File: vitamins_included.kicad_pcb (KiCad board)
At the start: 2 copper layers, 230.5 x 82 mm, 180 parts, among them J1 Speaker, J10 UTC16-G, J2 reset, J3 ISP, J4 reset, J5 Buzzer, J6 ISP, J9 UTC16-G, P3 WS2812, P4 SJ-43514-SMT, P6 WS2812, P8 SJ-43514-SMT, SW1 Socket, SW10 Socket, SW11 Socket, SW12 Socket, SW13 Socket, SW14 Socket, SW15 Socket, SW16 Socket, SW17 Socket, SW18 Socket, SW19 Socket, SW2 Socket, SW20 Socket, SW21 Socket, SW22 Socket, SW23 Socket, SW24 Socket, SW25 Socket, SW26 Socket, SW27 Socket, SW28 Socket, SW29 Socket, SW3 Socket, SW30 Socket, SW31 Socket, SW32 Socket, SW33 Socket, SW34 Socket, SW35 Socket, SW36 Socket, SW37 Socket, SW38 Socket, SW39 Socket, SW4 Socket, SW40 Socket, SW41 Socket, SW42 Socket, SW43 Socket, SW44 Socket, SW45 Socket, SW46 Socket, SW47 Socket, SW48 Socket, SW49 FSMSM, SW5 Socket, SW50 FSMSM, SW6 Socket, SW7 Socket, SW8 Socket, SW9 Socket, U1 ATMega32U4, U2 ATMega32U4, Y1 16MHz, Y2 16MHz

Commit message: Pre-cleanup
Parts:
- added J11: Conn_01x01, TestPoint:TestPoint_Pad_D1.5mm, B.Cu at (60.3, 18.9)
- added J12: Conn_01x01, TestPoint:TestPoint_Pad_D1.5mm, B.Cu at (69.9, 15.6)
- added J13: Conn_01x01, TestPoint:TestPoint_Pad_D1.5mm, B.Cu at (52.7, 6.50)
- added J14: Conn_01x01, TestPoint:TestPoint_Pad_D1.5mm, B.Cu at (61.3, 7.10)
- added J15: Conn_01x01, TestPoint:TestPoint_Pad_D1.5mm, B.Cu at (58.6, 3.30)
- added J16: Conn_01x01, TestPoint:TestPoint_Pad_D1.5mm, B.Cu at (78.0, 4.00)
- added J17: Conn_01x01, TestPoint:TestPoint_Pad_D1.5mm, B.Cu at (73.9, 8.50)
- added J18: Conn_01x01, TestPoint:TestPoint_Pad_D1.5mm, B.Cu at (175.7, 6.95)
- added J19: Conn_01x01, TestPoint:TestPoint_Pad_D1.5mm, B.Cu at (160.4, 14.8)
- added J20: Conn_01x01, TestPoint:TestPoint_Pad_D1.5mm, B.Cu at (150.1, 7.15)
- added J21: Conn_01x01, TestPoint:TestPoint_Pad_D1.5mm, B.Cu at (158.1, 7.30)
- added J22: Conn_01x01, TestPoint:TestPoint_Pad_D1.5mm, B.Cu at (156.2, 4.00)
- added J23: Conn_01x01, TestPoint:TestPoint_Pad_D1.5mm, B.Cu at (177.2, 11.4)
- added J24: Conn_01x01, TestPoint:TestPoint_Pad_D1.5mm, B.Cu at (160.7, 17.9)
- added J7: Conn_01x01, TestPoint:TestPoint_Pad_D1.5mm, B.Cu at (63.5, 17.9)
- added J8: Conn_01x01, TestPoint:TestPoint_Pad_D1.5mm, B.Cu at (167.6, 13.2)
- moved C4 1.16 mm to (55.6, 4.80), turned to 315 degrees
- moved C8 0.70 mm to (153.1, 4.30)
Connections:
- net /Right half/WD2812-in renamed /Right half/WS2812-in
- net /Right half/WD2812-out renamed /Right half/WS2812-out
- net /Right half/~RESET renamed /Right half/~Reset
- U1 pad 1: (no net) -> /Left half/PE6
- U1 pad 12: (no net) -> /Left half/PB7
- U1 pad 20: (no net) -> /Left half/PD2
- U1 pad 21: (no net) -> /Left half/PD3
- U1 pad 25: (no net) -> /Left half/PD4
- U1 pad 8: (no net) -> /Left half/PB0
- U2 pad 1: (no net) -> /Right half/PE6
- U2 pad 12: (no net) -> /Right half/PB7
- U2 pad 20: (no net) -> /Right half/PD2
- U2 pad 21: (no net) -> /Right half/PD3
- U2 pad 25: (no net) -> /Right half/PD4
- U2 pad 8: (no net) -> /Right half/PB0
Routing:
- net /Right half/SDA: track 75.6 -> 99.1 mm, vias 3 -> 4
- net /Left half/PD2: track 0.00 -> 12.0 mm, vias 0 -> 2
- net VCC: track 738.8 -> 749.7 mm
- net /Right half/PD2: track 0.00 -> 10.9 mm
- net /Right half/PD4: track 0.00 -> 7.41 mm
- net /Left half/PD3: track 0.00 -> 7.33 mm
- net /Left half/PD4: track 0.00 -> 5.10 mm
- net /Left half/PB0: track 0.00 -> 4.75 mm
- net /Right half/PB0: track 0.00 -> 4.42 mm
- net /Right half/PD3: track 0.00 -> 3.51 mm
- net VBUS: track 160.6 -> 157.5 mm
- net Net-(D35-Pad4): track 39.2 -> 36.1 mm
- net /Right half/PE6: track 0.00 -> 2.45 mm
- net /Left half/PE6: track 0.00 -> 2.42 mm
- net /Left half/MOSI: track 37.3 -> 35.3 mm
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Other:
- board text added: "-"
- board text added: "B0"
- board text added: "B7"
- board text added: "D -"
- board text added: "D2"
- board text added: "D3"
- board text added: "D4"
- board text added: "E6"
- board text removed: "+ D -"

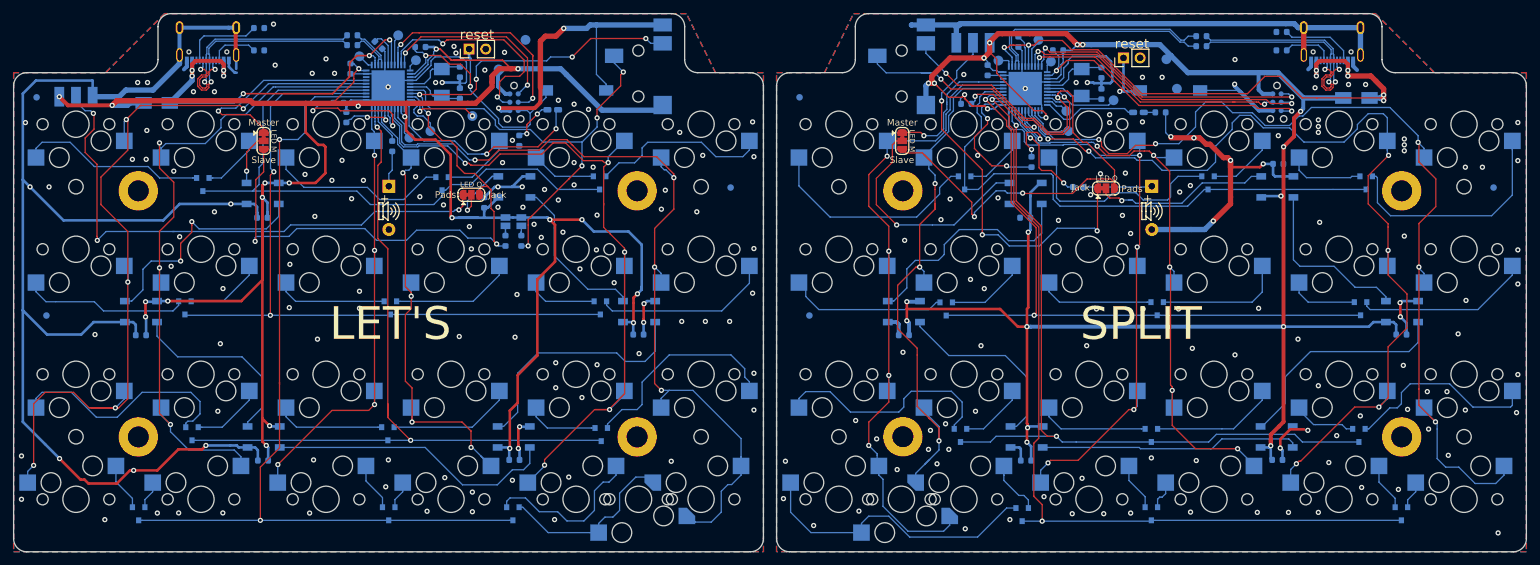
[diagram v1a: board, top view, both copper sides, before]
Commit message: Added footprint for AST1109MLTRQ buzzer
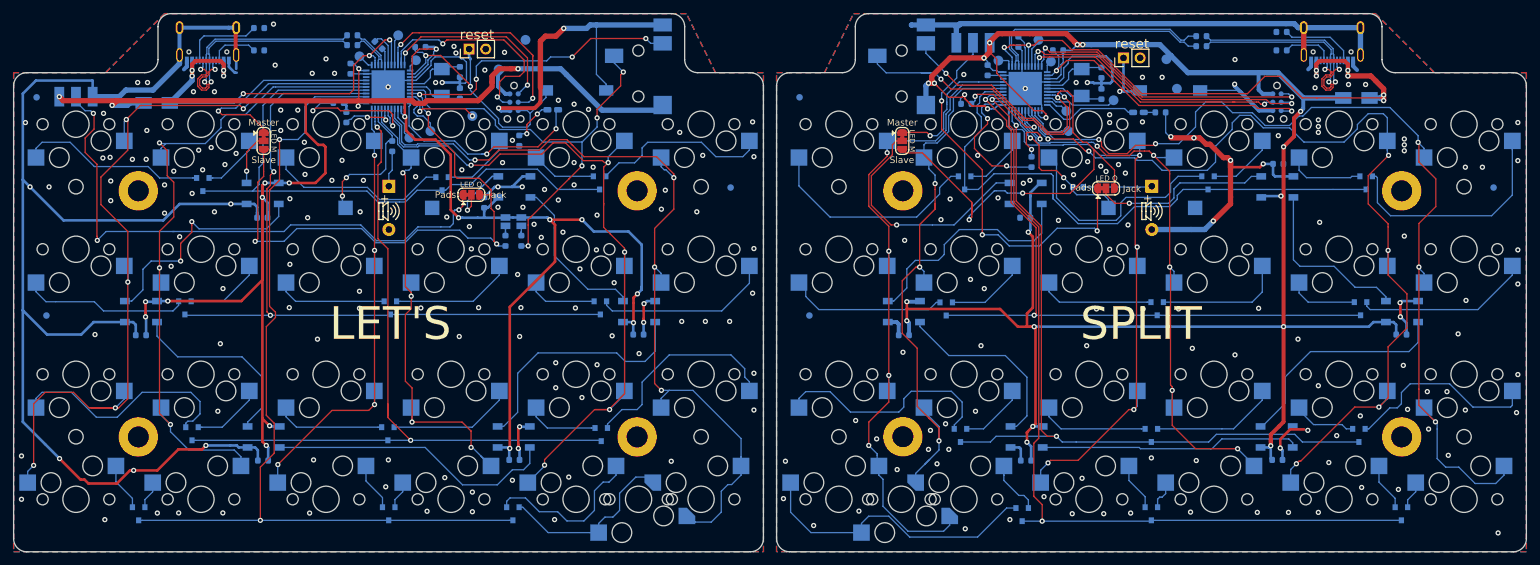
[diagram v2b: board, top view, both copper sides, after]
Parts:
- added J25: Buzzer_piezo, Buzzer_Beeper:Buzzer_Mallory_AST1109MLTRQ, B.Cu at (57.2, 29.6)
- added J26: Buzzer_piezo, Buzzer_Beeper:Buzzer_Mallory_AST1109MLTRQ, B.Cu at (173.4, 29.6)
- G*** (x2): footprint graphics:kiwi -> graphics:kiwi12.5mm
- P4, P8: footprint Connectors:SJ-4351X-SMT -> UJ31-CH-31-SMT-TR:SJ-4351X-SMT
- R1, R2, R6, R9: value 4k7 -> 4K7
- R17, R18, R19, R20: value 5k1 -> 5K1
- moved G*** 3.41 mm to (196.9, 31.7)
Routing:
- net /Left half/buzz: track 5.90 -> 23.5 mm, vias 0 -> 2
- net /Right half/buzz: track 16.7 -> 24.6 mm
- net VCC: track 749.7 -> 742.7 mm
- net /Left half/WS2812-out: track 84.7 -> 88.1 mm
- net /Right half/SDA: track 99.1 -> 102.4 mm
- net /Right half/row0: track 86.9 -> 90.2 mm
- net Net-(D14-Pad1): track 31.8 -> 34.1 mm
- net /Right half/col1: track 86.5 -> 88.2 mm
- net /Left half/row3: track 134.8 -> 136.2 mm
- net /Left half/~Reset: track 45.3 -> 43.9 mm
- net Net-(D35-Pad4): track 36.1 -> 37.2 mm
- net VBUS: track 157.5 -> 158.4 mm
- net /Left half/row0: track 95.7 -> 94.9 mm
- net GND: vias 226 -> 253
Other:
- board text added: "rev2.1"

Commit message: Modified reset switch footprint for better manufacturing, and added updated gerbers
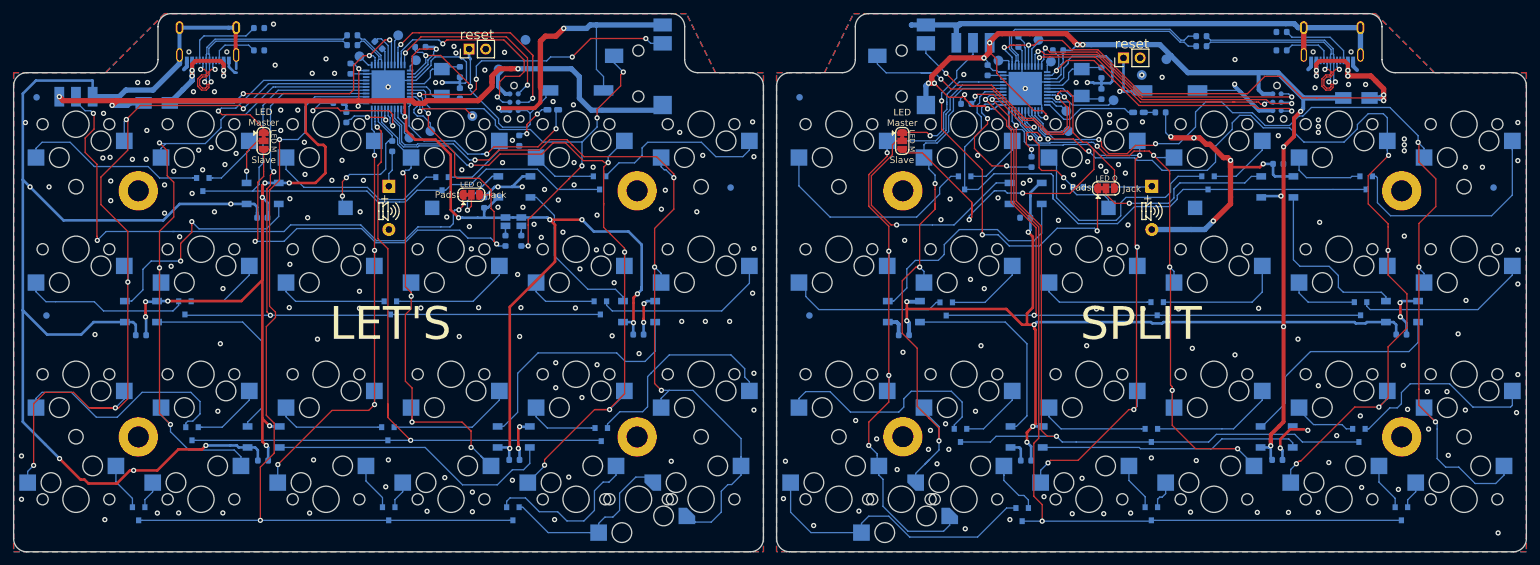
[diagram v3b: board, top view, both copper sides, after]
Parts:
- moved J23 5.75 mm to (171.9, 9.35)
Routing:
- net Net-(D36-Pad2): track 29.3 -> 31.8 mm
- net VCC: track 742.7 -> 744.6 mm
- net Net-(D30-Pad2): track 29.1 -> 31.0 mm
- net VBUS: track 158.4 -> 160.1 mm
- net Net-(D38-Pad4): track 26.6 -> 27.6 mm
- net Net-(D9-Pad2): track 32.4 -> 33.1 mm
- net GND: track 569.4 -> 569.2 mm, vias 253 -> 252
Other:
- board text added: "LED Master"
- board text removed: "Master"

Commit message: Added ESD protection to connectors
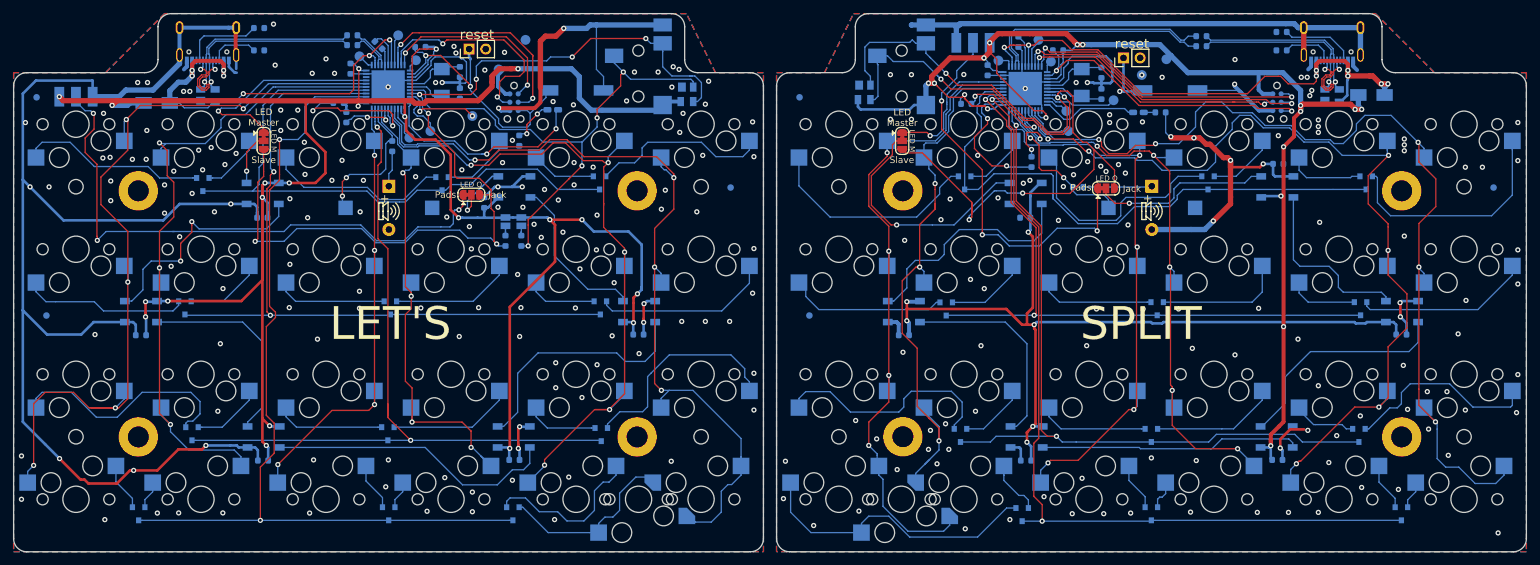
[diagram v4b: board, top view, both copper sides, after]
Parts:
- added D41: PRTR5V0U2X, Package_TO_SOT_SMD:SOT-143, B.Cu at (102.6, 12.3)
- added D42: PRTR5V0U2X, Package_TO_SOT_SMD:SOT-143, B.Cu at (29.6, 12.5)
- added D43: PRTR5V0U2X, Package_TO_SOT_SMD:SOT-143, B.Cu at (200.9, 12.5)
- added D44: PRTR5V0U2X, Package_TO_SOT_SMD:SOT-143, B.Cu at (129.6, 12.0)
- moved D26 2.34 mm to (206.9, 12.4)
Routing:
- net VCC: track 744.6 -> 767.4 mm, vias 41 -> 44
- net /Right half/SDA: track 102.4 -> 118.5 mm
- net /Left half/SDA: track 132.8 -> 147.5 mm
- net /Left half/SCL/D3: track 68.0 -> 80.1 mm
- net /Right half/SCL/D3: track 46.4 -> 52.8 mm
- net /Right half/col4: track 145.0 -> 140.1 mm
- net VBUS: track 160.1 -> 155.5 mm
- net /Right half/Dd+: track 32.6 -> 34.0 mm
- net /Right half/Dd-: track 34.1 -> 35.5 mm
- net /Left half/Dd-: track 35.5 -> 36.9 mm
- net /Left half/Dd+: track 35.0 -> 36.4 mm
- net /Right half/col5: track 146.4 -> 147.7 mm
- net GND: vias 252 -> 266

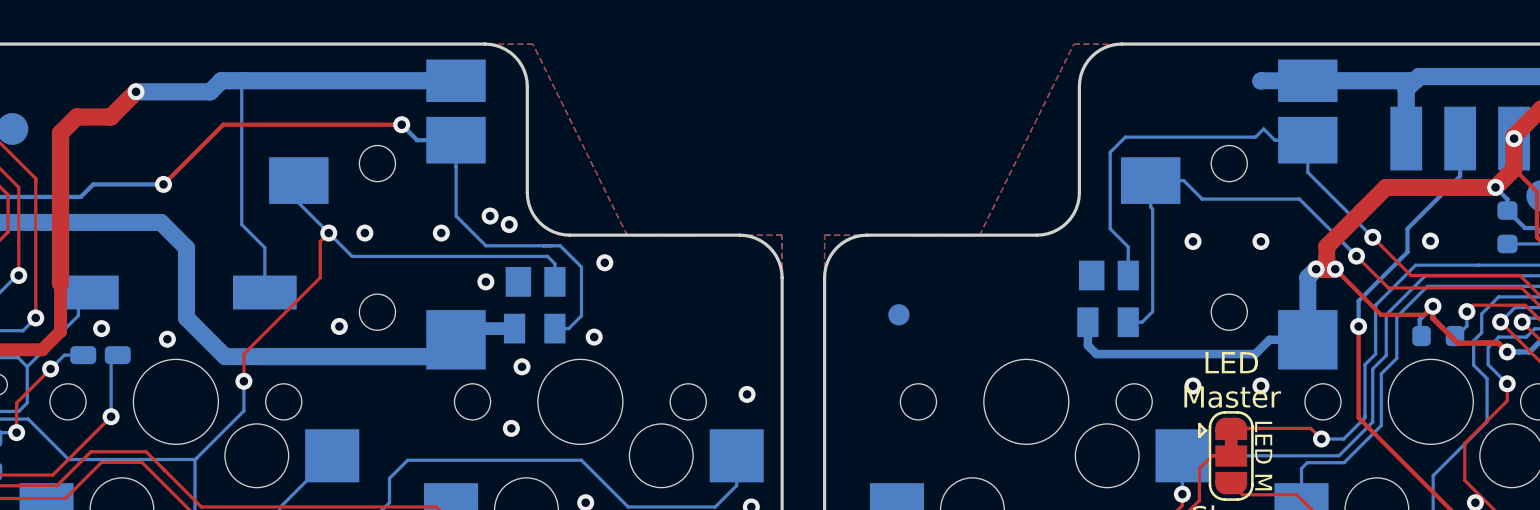
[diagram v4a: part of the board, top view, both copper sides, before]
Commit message: Added series resistors on TRRS
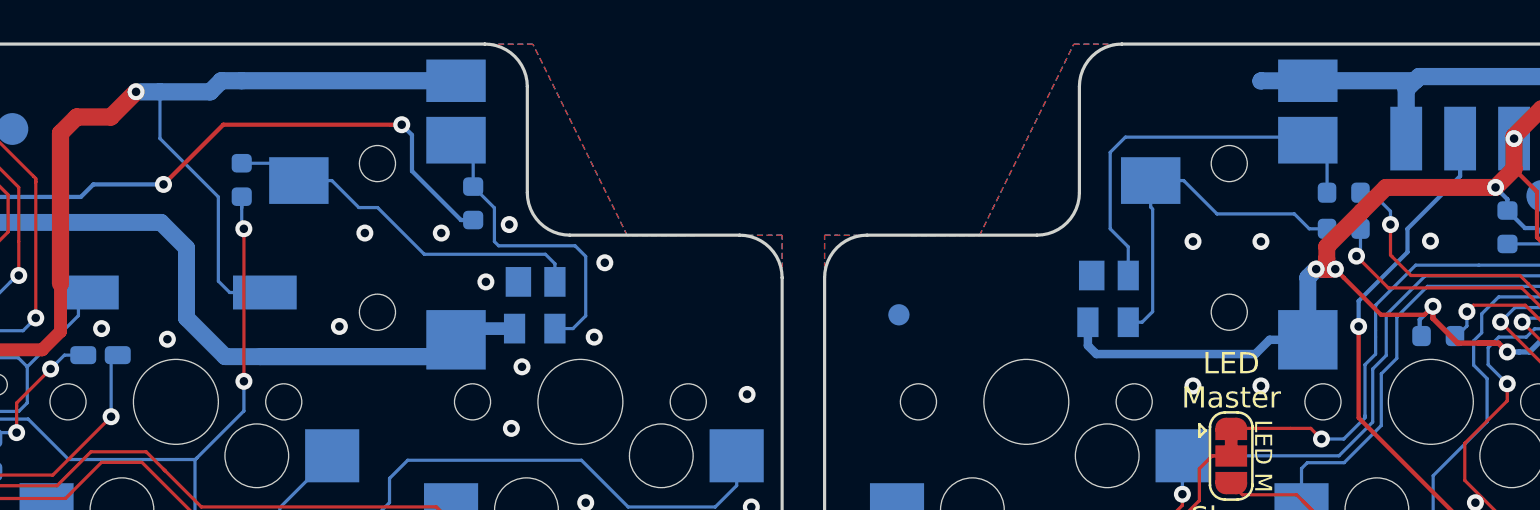
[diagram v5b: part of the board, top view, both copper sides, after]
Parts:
- added R21: 220R, Resistor_SMD:R_0603_1608Metric, B.Cu at (88.8, 6.40)
- added R22: 220R, Resistor_SMD:R_0603_1608Metric, B.Cu at (99.7, 7.50)
- added R23: 220R, Resistor_SMD:R_0603_1608Metric, B.Cu at (140.7, 8.70)
- added R24: 220R, Resistor_SMD:R_0603_1608Metric, B.Cu at (140.7, 7.00)
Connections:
- D41 pad 2: /Left half/SCL/D3 -> /Left half/Ring1
- D41 pad 3: /Left half/SDA -> /Left half/Ring2
- D44 pad 2: /Right half/SDA -> /Right half/Ring2
- D44 pad 3: /Right half/SCL/D3 -> /Right half/Ring1
- P4 pad R1: /Left half/SCL/D3 -> /Left half/Ring1
- P4 pad R2: /Left half/SDA -> /Left half/Ring2
- P8 pad R1: /Right half/SCL/D3 -> /Right half/Ring1
- P8 pad R2: /Right half/SDA -> /Right half/Ring2
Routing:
- net /Right half/SDA: track 118.5 -> 98.9 mm
- net /Right half/SCL/D3: track 52.8 -> 34.1 mm
- net /Right half/Ring2: track 0.00 -> 18.1 mm
- net /Left half/Ring1: track 0.00 -> 17.6 mm
- net /Right half/Ring1: track 0.00 -> 16.8 mm
- net /Left half/Ring2: track 0.00 -> 14.6 mm
- net /Left half/SCL/D3: track 80.1 -> 65.6 mm
- net /Left half/SDA: track 147.5 -> 136.2 mm
- net GND: track 569.2 -> 571.2 mm, vias 266 -> 265

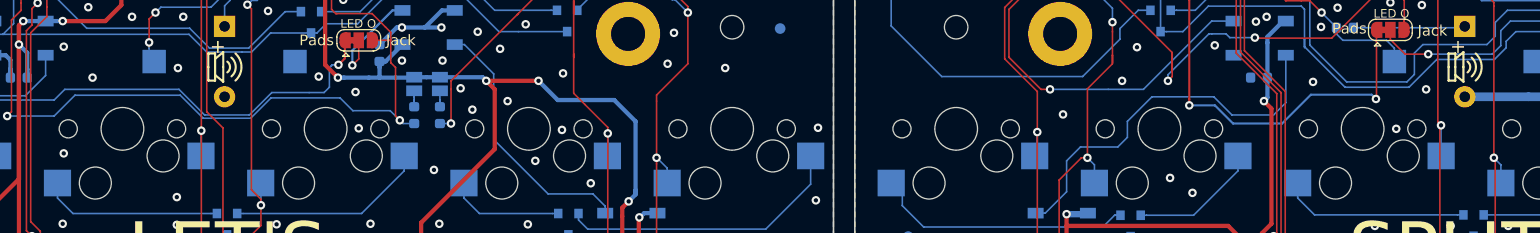
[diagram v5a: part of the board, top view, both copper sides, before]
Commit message: Added PE2 pull-down for dfu
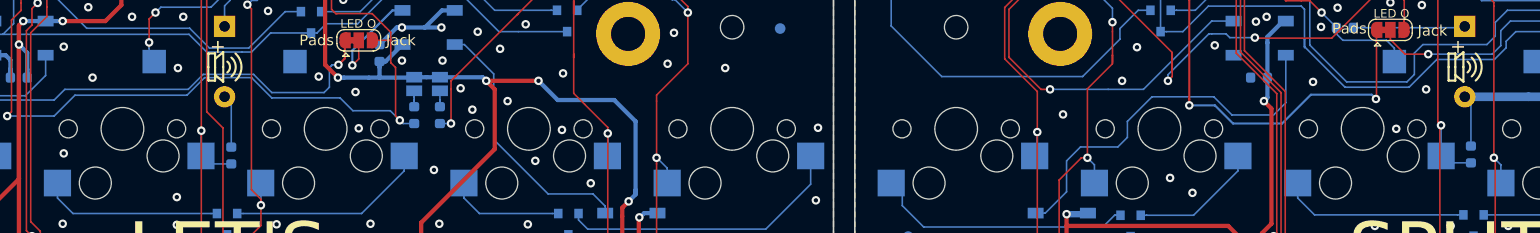
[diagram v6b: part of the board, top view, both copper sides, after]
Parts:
- added R25: 100k, Resistor_SMD:R_0603_1608Metric, B.Cu at (57.8, 38.4)
- added R26: 100k, Resistor_SMD:R_0603_1608Metric, B.Cu at (174.0, 38.3)
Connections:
- J10 pad A8: (no net) -> Net-(J10-PadA8)
- J10 pad B8: (no net) -> Net-(J10-PadB8)
- J9 pad A8: (no net) -> Net-(J9-PadA8)
- J9 pad B8: (no net) -> Net-(J9-PadB8)
- U1 pad 42: (no net) -> Net-(U1-Pad42)
- U2 pad 42: (no net) -> Net-(U2-Pad42)
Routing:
- net GND: track 571.2 -> 581.1 mm
- net /Left half/col2: track 71.0 -> 74.4 mm
- net /Right half/col2: track 92.8 -> 95.8 mm
- net /Left half/WS2812-out: track 88.1 -> 87.5 mm
